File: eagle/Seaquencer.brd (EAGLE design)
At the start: 94.9 x 72.4 mm, 45 parts, among them IC1 ATMEGA48/88/168, IC2 74HC595N

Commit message: Sequencer.brd: Add LED for Rotary Encdoer
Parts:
- added LED12, LED13: (no value), led:LED3MM
- added R1, R13: (no value), rcl:0207/7
- moved LED1 20.3 mm to (35.6, 64.8)
- moved R2 20.3 mm to (39.4, 61.0)
- moved LED11 6.48 mm to (90.2, 22.9), turned to 0 degrees
- moved LED10 4.02 mm to (90.2, 17.8), turned to 0 degrees
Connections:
- new net N$14: IC1.26, R1.2, R13.2
- new net N$32: LED12.K, R1.1
- new net N$37: LED13.A, R13.1
- net +3V3: now also LED12.A
- net GND: now also LED13.K
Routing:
- net +3V3: track 143.5 -> 123.2 mm
- net N$37: track 0.00 -> 13.8 mm
- net N$32: track 0.00 -> 9.72 mm
- net GND: track 402.6 -> 393.9 mm
- net RE_B: track 83.8 -> 76.2 mm
- net RE_A: track 94.0 -> 86.4 mm
- net N$8: track 66.0 -> 58.4 mm
- net N$12: track 55.9 -> 48.3 mm
- net N$9: track 40.6 -> 33.0 mm
- net RE_S: track 119.4 -> 111.8 mm
- net N$33: track 18.8 -> 12.7 mm
- net N$34: track 12.7 -> 15.2 mm
- net N$14: track 0.00 -> 2.54 mm
- net N$31: track 0.00 -> 2.54 mm

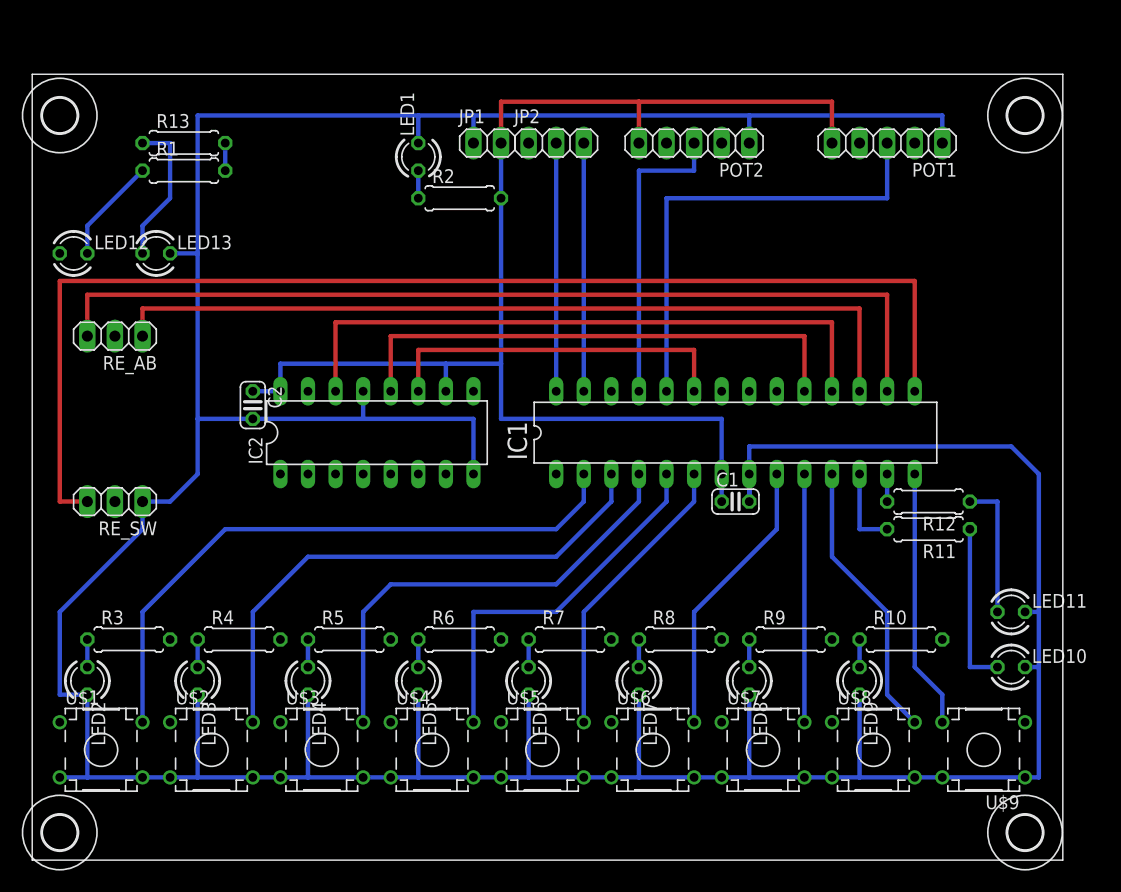
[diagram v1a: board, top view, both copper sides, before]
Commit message: Sequencer.brd: 部品再配置前
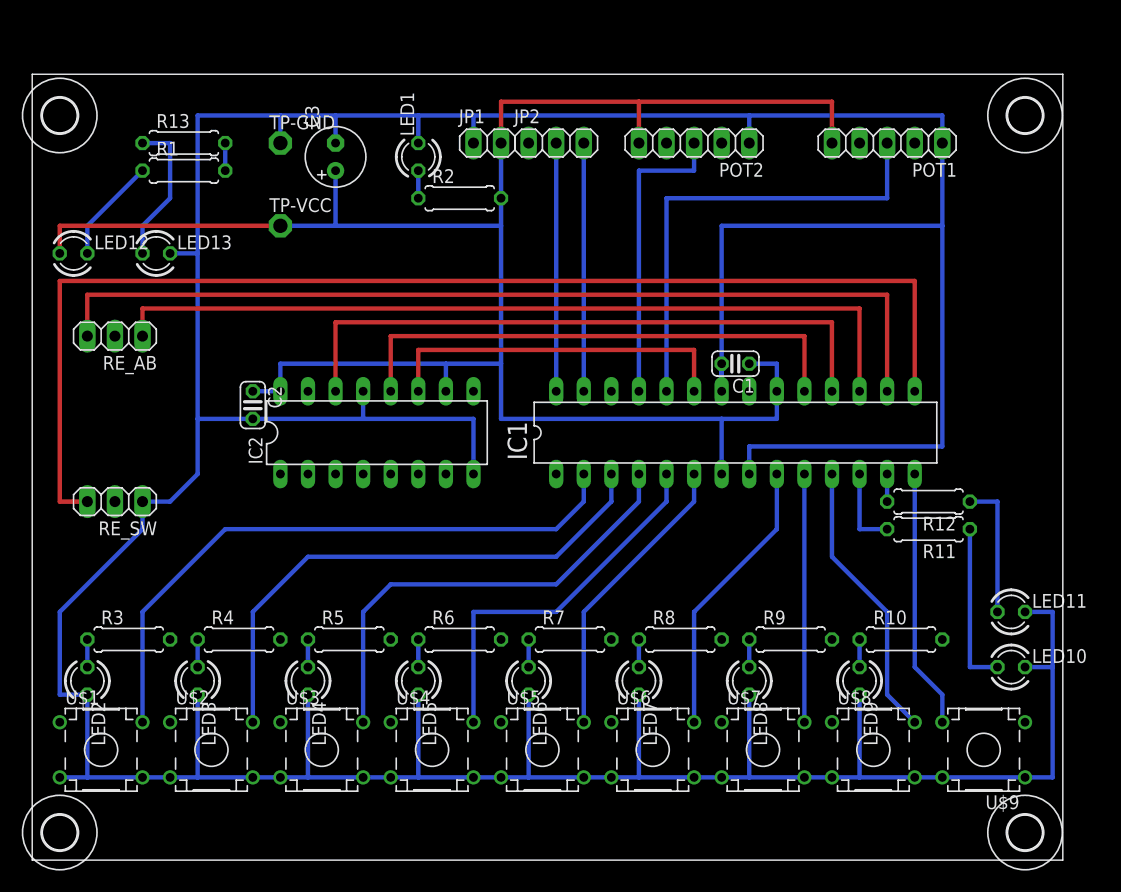
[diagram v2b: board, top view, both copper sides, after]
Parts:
- added C3: (no value), rcl:E2,5-6
- added TP-GND, TP-VCC: PTR1PAD1-13, testpad:P1-13
- moved C1 12.7 mm to (64.8, 45.7), turned to 180 degrees
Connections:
- removed net AVCC: IC1.20
- removed net GND2: IC1.22
- removed net RST: IC1.1, JP2.1
- net +3V3: now also C3.+, IC1.20, TP-VCC.TP
- net GND: now also C3.-, IC1.22, TP-GND.TP
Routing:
- net +3V3: track 123.2 -> 181.6 mm
- net GND: track 393.9 -> 441.1 mm
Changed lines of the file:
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@@
 <layer number="97" name="Info" color="7" fill="1" visible="no" active="no"/>
 <layer number="98" name="Guide" color="6" fill="1" visible="no" active="no"/>
-<layer number="100" name="Grid" color="11" fill="1" visible="no" active="yes"/>
-<layer number="101" name="Jumper" color="14" fill="1" visible="yes" active="yes"/>
+<layer number="100" name="Grid" color="11" fill="1" visible="yes" active="yes"/>
+<layer number="101" name="Jumper" color="14" fill="1" visible="no" active="yes"/>
 <layer number="200" name="200bmp" color="1" fill="10" visible="no" active="no"/>
 <layer number="201" name="tNamesOnPCB" color="5" fill="1" visible="yes" active="yes"/>
@@
 <wire x1="35.56" y1="35.56" x2="73.66" y2="20.32" width="0.4064" layer="101"/>
 <wire x1="38.1" y1="35.56" x2="83.82" y2="20.32" width="0.4064" layer="101"/>
-<wire x1="45.72" y1="66.04" x2="48.26" y2="35.56" width="0.4064" layer="101"/>
 <wire x1="53.34" y1="43.18" x2="17.78" y2="63.5" width="0.4064" layer="101"/>
-<wire x1="2.54" y1="55.88" x2="20.32" y2="43.18" width="0.4064" layer="101"/>
 </plain>
 <attributes>
@@
 <element name="U$13" library="holes" package="3,2" value="" x="91.44" y="68.58"/>
 <element name="IC1" library="mylib" package="DIL28-3" value="ATMEGA48/88/168" x="63.5" y="39.37"/>
-<element name="C1" library="rcl" package="C025-024X044" value="" x="64.77" y="33.02"/>
+<element name="C1" library="rcl" package="C025-024X044" value="" x="64.77" y="45.72" rot="R180"/>
 <element name="RE_AB" library="pinhead" package="1X03" value="" x="7.62" y="48.26" rot="R180"/>
 <element name="RE_SW" library="pinhead" package="1X03" value="" x="7.62" y="33.02" rot="R180"/>
@@
 <element name="LED13" library="led" package="LED3MM" value="" x="11.43" y="55.88"/>
 <element name="R13" library="rcl" package="0207/7" value="" x="13.97" y="66.04"/>
+<element name="C3" library="rcl" package="E2,5-6" value="" x="27.94" y="64.77" rot="R90"/>
+<element name="TP-GND" library="testpad" package="P1-13" value="PTR1PAD1-13" x="22.86" y="66.04">
+<attribute name="TP_SIGNAL_NAME" value="" x="22.86" y="66.04" size="1.778" layer="27" display="off"/>
+</element>
+<element name="TP-VCC" library="testpad" package="P1-13" value="PTR1PAD1-13" x="22.86" y="58.42">
+<attribute name="TP_SIGNAL_NAME" value="" x="22.86" y="58.42" size="1.778" layer="27" display="off"/>
+</element>
 </elements>
 <signals>
-<signal name="AVCC">
-<contactref element="IC1" pad="20"/>
-</signal>
 <signal name="GND">
 <contactref element="JP1" pad="1"/>
@@
 <contactref element="C1" pad="2"/>
 <wire x1="40.64" y1="40.64" x2="40.64" y2="35.56" width="0.4064" layer="16"/>
-<wire x1="66.04" y1="35.56" x2="66.04" y2="33.02" width="0.4064" layer="16"/>
 <contactref element="RE_SW" pad="1"/>
 <wire x1="20.32" y1="40.64" x2="15.24" y2="40.64" width="0.4064" layer="16"/>
@@
 <wire x1="30.48" y1="40.64" x2="30.48" y2="43.18" width="0.4064" layer="16"/>
 <wire x1="40.64" y1="40.64" x2="30.48" y2="40.64" width="0.4064" layer="16"/>
-<wire x1="15.24" y1="68.58" x2="35.56" y2="68.58" width="0.4064" layer="16"/>
+<wire x1="15.24" y1="68.58" x2="22.86" y2="68.58" width="0.4064" layer="16"/>
+<wire x1="22.86" y1="68.58" x2="27.94" y2="68.58" width="0.4064" layer="16"/>
+<wire x1="27.94" y1="68.58" x2="35.56" y2="68.58" width="0.4064" layer="16"/>
 <wire x1="35.56" y1="68.58" x2="40.64" y2="68.58" width="0.4064" layer="16"/>
 <wire x1="35.56" y1="66.04" x2="35.56" y2="68.58" width="0.4064" layer="16"/>
@@
 <wire x1="12.7" y1="33.02" x2="15.24" y2="35.56" width="0.4064" layer="16"/>
 <wire x1="15.24" y1="35.56" x2="15.24" y2="40.64" width="0.4064" layer="16"/>
-<wire x1="91.44" y1="7.62" x2="92.71" y2="7.62" width="0.4064" layer="16"/>
-<wire x1="92.71" y1="7.62" x2="92.71" y2="17.78" width="0.4064" layer="16"/>
-<wire x1="92.71" y1="17.78" x2="92.71" y2="22.86" width="0.4064" layer="16"/>
-<wire x1="92.71" y1="22.86" x2="91.44" y2="22.86" width="0.4064" layer="16"/>
-<wire x1="91.44" y1="17.78" x2="92.71" y2="17.78" width="0.4064" layer="16"/>
 <wire x1="91.44" y1="7.62" x2="83.82" y2="7.62" width="0.4064" layer="16"/>
-<wire x1="66.04" y1="33.02" x2="66.04" y2="38.1" width="0.4064" layer="16"/>
-<wire x1="66.04" y1="38.1" x2="90.17" y2="38.1" width="0.4064" layer="16"/>
-<wire x1="90.17" y1="38.1" x2="92.71" y2="35.56" width="0.4064" layer="16"/>
-<wire x1="92.71" y1="35.56" x2="92.71" y2="22.86" width="0.4064" layer="16"/>
+<contactref element="C3" pad="-"/>
+<contactref element="TP-GND" pad="TP"/>
+<wire x1="27.94" y1="66.04" x2="27.94" y2="68.58" width="0.4064" layer="16"/>
+<wire x1="22.86" y1="66.04" x2="22.86" y2="68.58" width="0.4064" layer="16"/>
+<contactref element="IC1" pad="22"/>
+<wire x1="63.5" y1="43.18" x2="63.5" y2="45.72" width="0.4064" layer="16"/>
+<wire x1="63.5" y1="43.18" x2="63.5" y2="58.42" width="0.4064" layer="16"/>
+<wire x1="63.5" y1="58.42" x2="83.82" y2="58.42" width="0.4064" layer="16"/>
+<wire x1="83.82" y1="58.42" x2="83.82" y2="66.04" width="0.4064" layer="16"/>
+<wire x1="66.04" y1="35.56" x2="66.04" y2="38.1" width="0.4064" layer="16"/>
+<wire x1="66.04" y1="38.1" x2="83.82" y2="38.1" width="0.4064" layer="16"/>
+<wire x1="83.82" y1="38.1" x2="83.82" y2="58.42" width="0.4064" layer="16"/>
+<wire x1="91.44" y1="7.62" x2="93.98" y2="7.62" width="0.4064" layer="16"/>
+<wire x1="93.98" y1="7.62" x2="93.98" y2="17.78" width="0.4064" layer="16"/>
+<wire x1="93.98" y1="17.78" x2="93.98" y2="22.86" width="0.4064" layer="16"/>
+<wire x1="93.98" y1="22.86" x2="91.44" y2="22.86" width="0.4064" layer="16"/>
+<wire x1="91.44" y1="17.78" x2="93.98" y2="17.78" width="0.4064" layer="16"/>
 </signal>
 <signal name="N$1">
@@
 <contactref element="C1" pad="1"/>
 <wire x1="22.86" y1="43.18" x2="20.32" y2="43.18" width="0.4064" layer="16"/>
-<wire x1="63.5" y1="35.56" x2="63.5" y2="33.02" width="0.4064" layer="16"/>
 <wire x1="63.5" y1="35.56" x2="63.5" y2="40.64" width="0.4064" layer="16"/>
 <wire x1="63.5" y1="40.64" x2="43.18" y2="40.64" width="0.4064" layer="16"/>
 <contactref element="IC2" pad="10"/>
 <wire x1="43.18" y1="66.04" x2="43.18" y2="60.96" width="0.4064" layer="16"/>
-<wire x1="43.18" y1="60.96" x2="43.18" y2="45.72" width="0.4064" layer="16"/>
+<wire x1="43.18" y1="60.96" x2="43.18" y2="58.42" width="0.4064" layer="16"/>
+<wire x1="43.18" y1="58.42" x2="43.18" y2="45.72" width="0.4064" layer="16"/>
 <wire x1="43.18" y1="45.72" x2="43.18" y2="40.64" width="0.4064" layer="16"/>
 <wire x1="38.1" y1="43.18" x2="38.1" y2="45.72" width="0.4064" layer="16"/>
@@
 <wire x1="22.86" y1="43.18" x2="22.86" y2="45.72" width="0.4064" layer="16"/>
 <wire x1="22.86" y1="45.72" x2="38.1" y2="45.72" width="0.4064" layer="16"/>
-<wire x1="2.54" y1="55.88" x2="20.32" y2="43.18" width="0" layer="19" extent="1-1"/>
+<contactref element="C3" pad="+"/>
+<contactref element="TP-VCC" pad="TP"/>
+<wire x1="22.86" y1="58.42" x2="27.94" y2="58.42" width="0.4064" layer="16"/>
+<wire x1="27.94" y1="58.42" x2="43.18" y2="58.42" width="0.4064" layer="16"/>
+<wire x1="27.94" y1="63.5" x2="27.94" y2="58.42" width="0.4064" layer="16"/>
+<wire x1="2.54" y1="55.88" x2="2.54" y2="58.42" width="0.4064" layer="1"/>
+<wire x1="2.54" y1="58.42" x2="22.86" y2="58.42" width="0.4064" layer="1"/>
+<contactref element="IC1" pad="20"/>
+<wire x1="68.58" y1="43.18" x2="68.58" y2="40.64" width="0.4064" layer="16"/>
+<wire x1="68.58" y1="40.64" x2="63.5" y2="40.64" width="0.4064" layer="16"/>
+<wire x1="66.04" y1="45.72" x2="68.58" y2="45.72" width="0.4064" layer="16"/>
+<wire x1="68.58" y1="45.72" x2="68.58" y2="43.18" width="0.4064" layer="16"/>
 </signal>
 <signal name="N$15">
@@
 <wire x1="55.88" y1="33.02" x2="48.26" y2="25.4" width="0.4064" layer="16"/>
 </signal>
-<signal name="GND2">
-<contactref element="IC1" pad="22"/>
-</signal>
 <signal name="RE_S">
 <contactref element="RE_SW" pad="3"/>
@@
 <wire x1="50.8" y1="43.18" x2="50.8" y2="66.04" width="0.4064" layer="16"/>
 </signal>
-<signal name="RST">
-<contactref element="IC1" pad="1"/>
-<contactref element="JP2" pad="1"/>
-<wire x1="48.26" y1="35.56" x2="45.72" y2="66.04" width="0" layer="19" extent="1-1"/>
-</signal>
 <signal name="N$8">

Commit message: 回路図、基板図： Valueを設定
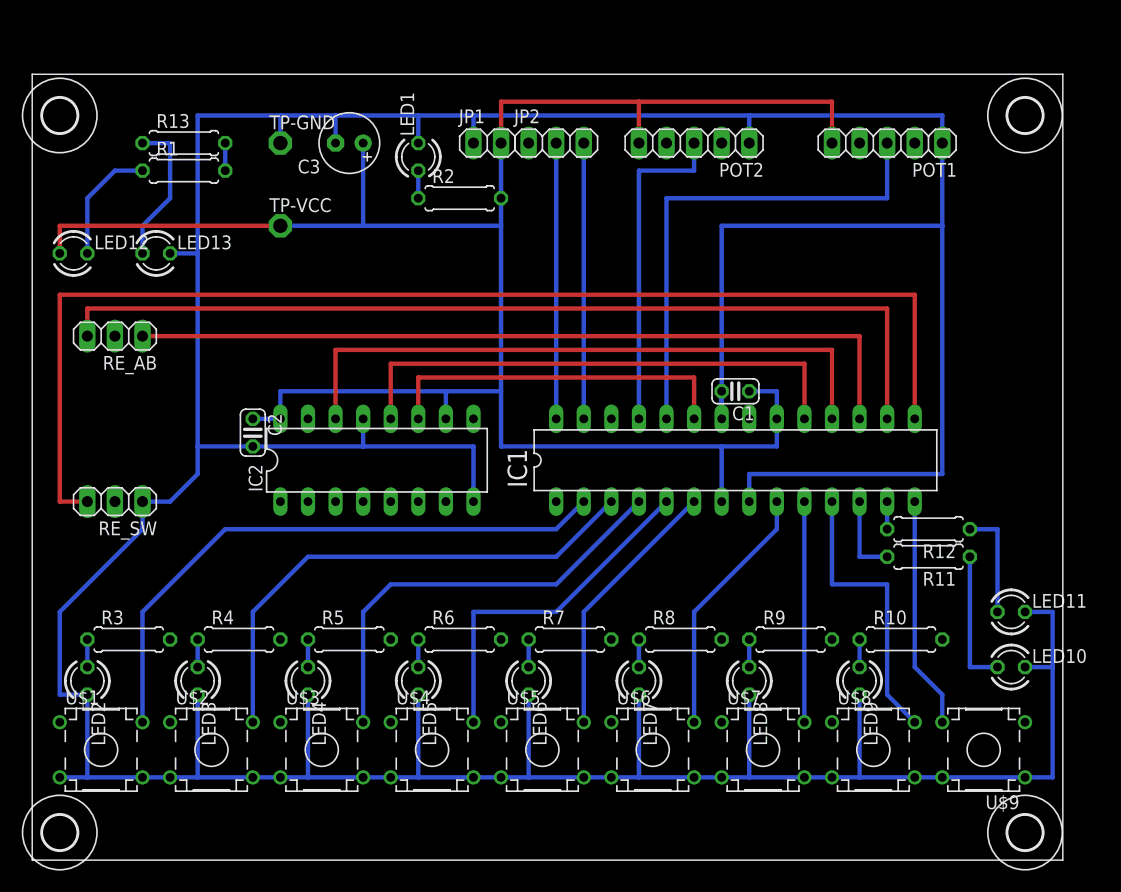
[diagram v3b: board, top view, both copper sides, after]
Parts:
- C1, C2: value (none) -> 0.1uF
- C3: value (none) -> 47uF
- R1, R10, R11, R12, R13, R2, R3, R4, R5, R6, R7, R8, R9: value (none) -> 1.5k
- moved R12 2.54 mm to (82.5, 30.5)
- moved C1 2.54 mm to (64.8, 43.2)
- moved C2 2.54 mm to (20.3, 39.4)
- moved IC1 2.54 mm to (63.5, 36.8)
- moved IC2 2.54 mm to (31.8, 36.8)
- moved R11 2.54 mm to (82.5, 27.9)
- moved C3 1.80 mm to (29.2, 66.0), turned to 180 degrees
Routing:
- net GND: track 441.1 -> 446.2 mm
- net +3V3: track 181.6 -> 186.7 mm
- net RE_B: track 76.2 -> 73.7 mm
- net N$41: track 42.3 -> 39.8 mm
- net N$33: track 12.7 -> 10.2 mm
- net SDA: track 22.9 -> 25.4 mm
- net SCL: track 22.9 -> 25.4 mm
- net N$7: track 34.7 -> 32.1 mm
- net N$6: track 27.1 -> 24.5 mm
- net N$5: track 26.0 -> 23.5 mm
- net N$4: track 22.9 -> 20.3 mm
- net N$34: track 15.2 -> 12.7 mm
- net N$2: track 49.9 -> 47.4 mm
- net N$13: track 23.9 -> 21.4 mm
- net N$11: track 27.9 -> 30.5 mm
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
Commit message: Sequencer.brd: Rotary Encoderの位置を移動
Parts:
- moved RE_SW 2.54 mm to (7.62, 30.5)
- moved RE_AB 2.54 mm to (7.62, 45.7)
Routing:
- net RE_A: track 86.4 -> 88.9 mm
- net RE_B: track 73.7 -> 76.2 mm
- net RE_S: track 111.8 -> 112.8 mm
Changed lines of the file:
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@@
 <element name="IC1" library="mylib" package="DIL28-3" value="ATMEGA48/88/168" x="63.5" y="36.83"/>
 <element name="C1" library="rcl" package="C025-024X044" value="0.1uF" x="64.77" y="43.18" rot="R180"/>
-<element name="RE_AB" library="pinhead" package="1X03" value="" x="7.62" y="48.26" rot="R180"/>
-<element name="RE_SW" library="pinhead" package="1X03" value="" x="7.62" y="33.02" rot="R180"/>
+<element name="RE_AB" library="pinhead" package="1X03" value="" x="7.62" y="45.72" rot="R180"/>
+<element name="RE_SW" library="pinhead" package="1X03" value="" x="7.62" y="30.48" rot="R180"/>
 <element name="JP2" library="pinhead" package="1X03" value="I2C" x="48.26" y="66.04"/>
 <element name="POT1" library="pinhead" package="1X05" value="" x="78.74" y="66.04" rot="R180"/>
@@
 <contactref element="LED13" pad="K"/>
 <wire x1="12.7" y1="55.88" x2="15.24" y2="55.88" width="0.4064" layer="16"/>
-<wire x1="10.16" y1="33.02" x2="10.16" y2="30.48" width="0.4064" layer="16"/>
-<wire x1="10.16" y1="30.48" x2="2.54" y2="22.86" width="0.4064" layer="16"/>
 <wire x1="2.54" y1="22.86" x2="2.54" y2="15.24" width="0.4064" layer="16"/>
-<wire x1="10.16" y1="33.02" x2="12.7" y2="33.02" width="0.4064" layer="16"/>
-<wire x1="12.7" y1="33.02" x2="15.24" y2="35.56" width="0.4064" layer="16"/>
 <wire x1="15.24" y1="35.56" x2="15.24" y2="38.1" width="0.4064" layer="16"/>
 <wire x1="91.44" y1="7.62" x2="83.82" y2="7.62" width="0.4064" layer="16"/>
@@
 <wire x1="30.48" y1="40.64" x2="30.48" y2="38.1" width="0.4064" layer="16"/>
 <wire x1="27.94" y1="66.04" x2="27.94" y2="68.58" width="0.4064" layer="16"/>
+<wire x1="10.16" y1="30.48" x2="15.24" y2="35.56" width="0.4064" layer="16"/>
+<wire x1="10.16" y1="30.48" x2="10.16" y2="27.94" width="0.4064" layer="16"/>
+<wire x1="10.16" y1="27.94" x2="5.08" y2="22.86" width="0.4064" layer="16"/>
+<wire x1="5.08" y1="22.86" x2="2.54" y2="22.86" width="0.4064" layer="16"/>
 </signal>
 <signal name="N$1">
@@
 <wire x1="76.2" y1="40.64" x2="76.2" y2="48.26" width="0.4064" layer="1"/>
 <wire x1="76.2" y1="48.26" x2="10.16" y2="48.26" width="0.4064" layer="1"/>
+<wire x1="10.16" y1="48.26" x2="10.16" y2="45.72" width="0.4064" layer="1"/>
 </signal>
 <signal name="RE_A">
@@
 <wire x1="78.74" y1="40.64" x2="78.74" y2="50.8" width="0.4064" layer="1"/>
 <wire x1="78.74" y1="50.8" x2="5.08" y2="50.8" width="0.4064" layer="1"/>
-<wire x1="5.08" y1="50.8" x2="5.08" y2="48.26" width="0.4064" layer="1"/>
+<wire x1="5.08" y1="50.8" x2="5.08" y2="45.72" width="0.4064" layer="1"/>
 </signal>
 <signal name="N$41">
@@
 <wire x1="81.28" y1="52.07" x2="2.54" y2="52.07" width="0.4064" layer="1"/>
 <wire x1="2.54" y1="52.07" x2="2.54" y2="33.02" width="0.4064" layer="1"/>
-<wire x1="2.54" y1="33.02" x2="5.08" y2="33.02" width="0.4064" layer="1"/>
+<wire x1="2.54" y1="33.02" x2="5.08" y2="30.48" width="0.4064" layer="1"/>
 </signal>
 <signal name="N$35">

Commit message: 抵抗値変更
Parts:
- R1, R11, R2: value 1.5k -> 2k
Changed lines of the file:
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@@
 <element name="JP1" library="pinhead" package="1X02" value="3.3VIN" x="41.91" y="66.04"/>
 <element name="IC2" library="74xx-eu" package="DIL16" value="74HC595N" x="31.75" y="36.83"/>
-<element name="R2" library="rcl" package="0207/7" value="1.5k" x="39.37" y="60.96"/>
+<element name="R2" library="rcl" package="0207/7" value="2k" x="39.37" y="60.96"/>
 <element name="LED1" library="led" package="LED3MM" value="" x="35.56" y="64.77" rot="R90"/>
 <element name="LED2" library="led" package="LED3MM" value="" x="5.08" y="16.51" rot="R270"/>
@@
 <element name="LED8" library="led" package="LED3MM" value="" x="66.04" y="16.51" rot="R270"/>
 <element name="LED9" library="led" package="LED3MM" value="" x="76.2" y="16.51" rot="R270"/>
-<element name="R11" library="rcl" package="0207/7" value="1.5k" x="82.55" y="27.94" rot="R180"/>
+<element name="R11" library="rcl" package="0207/7" value="2k" x="82.55" y="27.94" rot="R180"/>
 <element name="R12" library="rcl" package="0207/7" value="1.5k" x="82.55" y="30.48" rot="R180"/>
 <element name="LED10" library="led" package="LED3MM" value="" x="90.17" y="17.78"/>
@@
 <element name="POT2" library="pinhead" package="1X05" value="" x="60.96" y="66.04" rot="R180"/>
 <element name="LED12" library="led" package="LED3MM" value="" x="3.81" y="55.88"/>
-<element name="R1" library="rcl" package="0207/7" value="1.5k" x="13.97" y="63.5"/>
+<element name="R1" library="rcl" package="0207/7" value="2k" x="13.97" y="63.5"/>
 <element name="LED13" library="led" package="LED3MM" value="" x="11.43" y="55.88"/>
 <element name="R13" library="rcl" package="0207/7" value="1.5k" x="13.97" y="66.04"/>
